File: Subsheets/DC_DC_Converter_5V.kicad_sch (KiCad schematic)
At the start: 30 parts

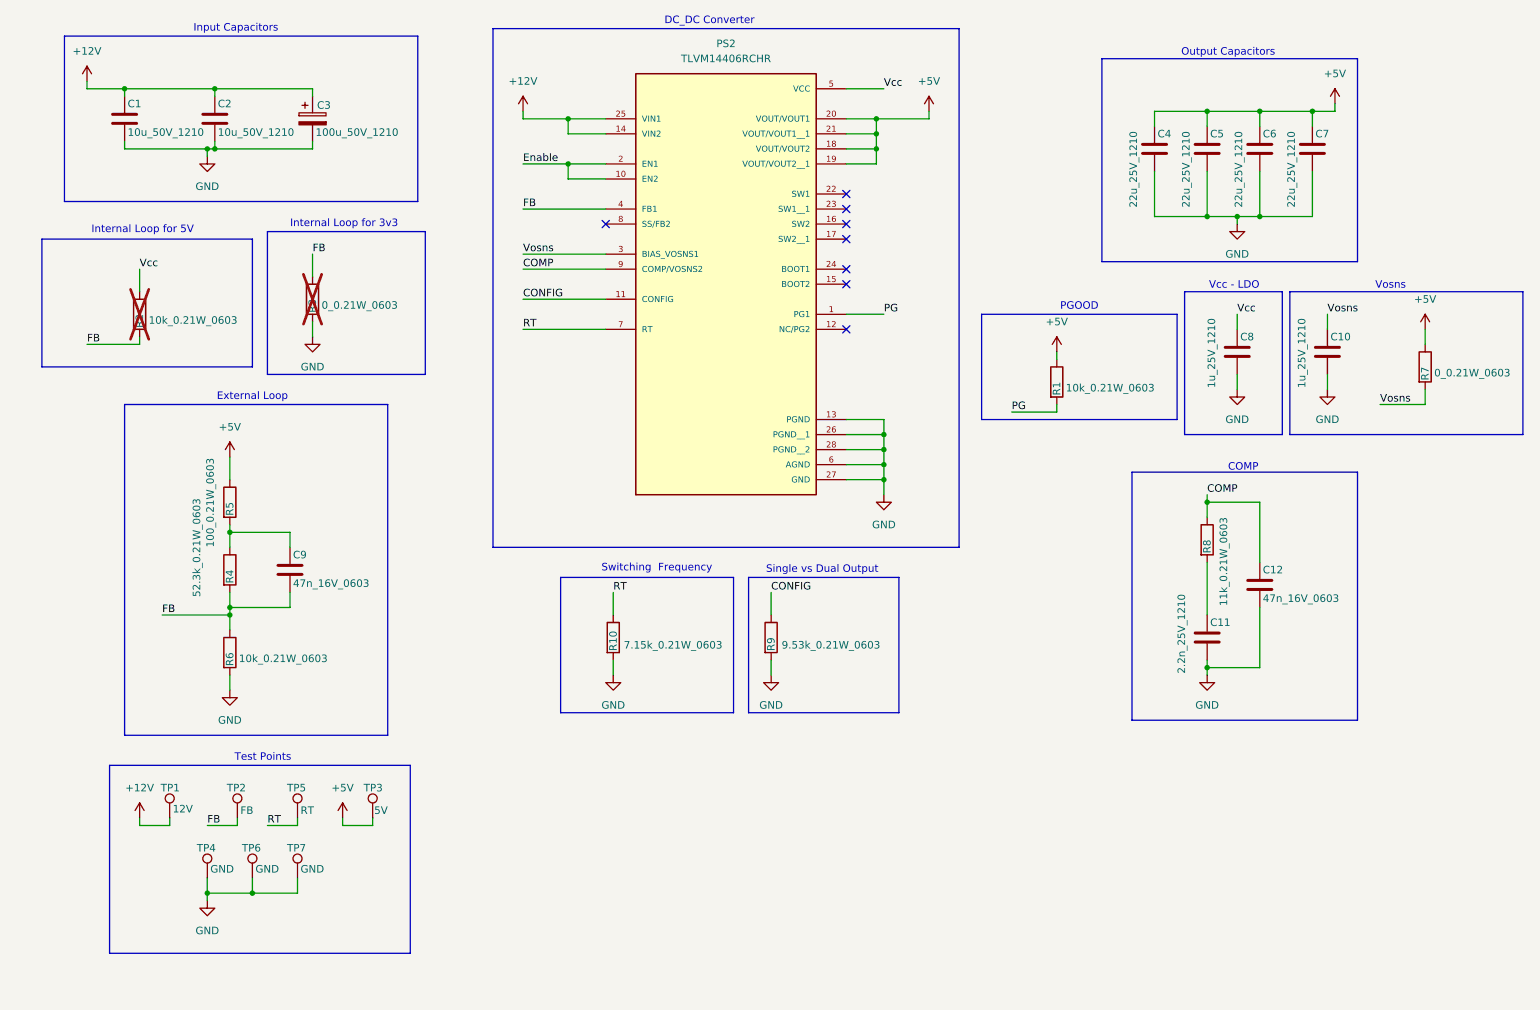
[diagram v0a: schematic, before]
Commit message: Layout import and schema fixes.
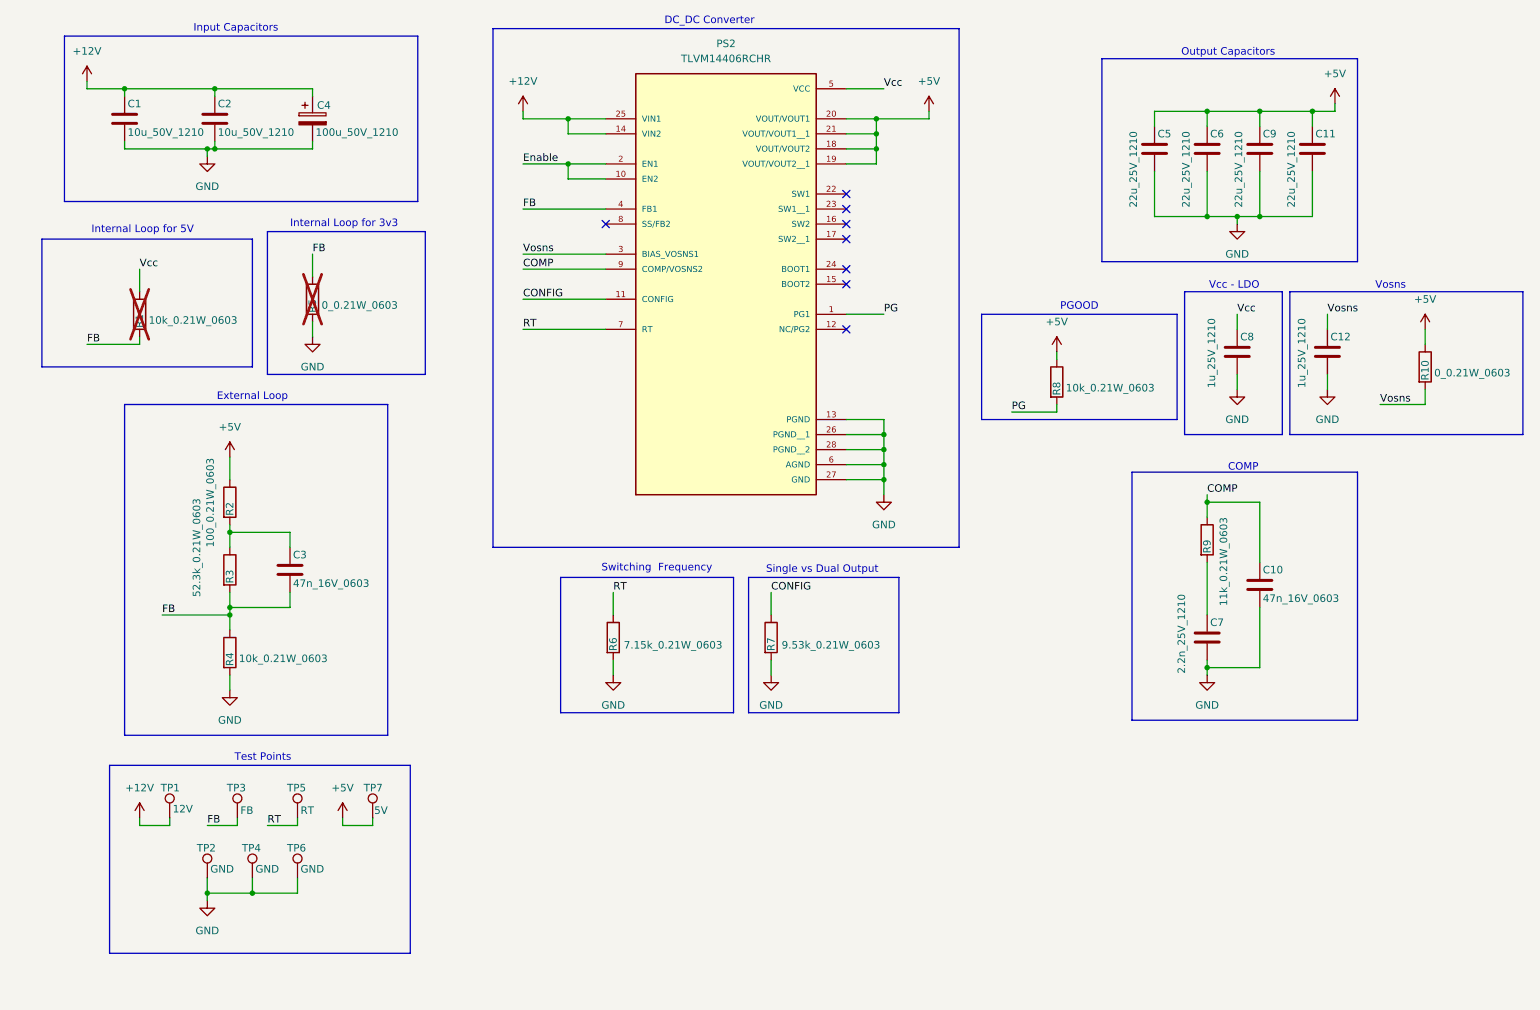
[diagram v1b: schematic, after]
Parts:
- C7: renamed from C11; footprint (none) -> Capacitor_SMD:C_1210_3225Metric
- PS2: footprint TLVM14406RCHR:CONV_TLVM14406RCHR -> footprints:CONV_TLVM14406RCHR; Manufacturer Part Number (none) -> TLVM14406RCHR; Price (none) -> 742; Vendor Link (none) -> https://www.digikey.in/en/products/detail/texas-instruments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; Vendor Part Number (none) -> 296-TLVM14406RCHRCT-ND
- R1: renamed from R2; footprint (none) -> Resistor_SMD:R_0603_1608Metric_Pad0.98x0.95mm_HandSolder; MANUFACTURER (none) -> Vishay Dale; Manufacturer Part Number (none) -> CRCW060310K0FKEAHP; Price (none) -> 6.01; Vendor Link (none) -> https://www.digikey.in/en/products/detail/vishay-dale/CRCW0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; Vendor Part Number (none) -> 541-10.0KSCT-ND
- R10: renamed from R7; footprint (none) -> Resistor_SMD:R_0603_1608Metric_Pad0.98x0.95mm_HandSolder; MANUFACTURER (none) -> Vishay Dale; Manufacturer Part Number (none) -> CRCW06030000Z0EAHP; Price (none) -> 4.86; Vendor Link (none) -> https://www.digikey.in/en/products/detail/vishay-dale/CRCW0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; Vendor Part Number (none) -> 541-0.0SBCT-ND
- R2: renamed from R5; footprint (none) -> Resistor_SMD:R_0603_1608Metric_Pad0.98x0.95mm_HandSolder; MANUFACTURER (none) -> Vishay Dale; Manufacturer Part Number (none) -> CRCW0603100RFKEAHP; Price (none) -> 6.01; Vendor Link (none) -> https://www.digikey.in/en/products/detail/vishay-dale/CRCW0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; Vendor Part Number (none) -> 541-100SCT-ND
- R3: renamed from R4; footprint (none) -> Resistor_SMD:R_0603_1608Metric_Pad0.98x0.95mm_HandSolder; MANUFACTURER (none) -> Vishay Dale; Manufacturer Part Number (none) -> CRCW060352K3FKEAC; Price (none) -> 2.56; Vendor Link (none) -> https://www.digikey.in/en/products/detail/vishay-dale/CRCW0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; Vendor Part Number (none) -> 541-5470-1-ND
- R4: renamed from R6; footprint (none) -> Resistor_SMD:R_0603_1608Metric_Pad0.98x0.95mm_HandSolder; MANUFACTURER (none) -> Vishay Dale; Manufacturer Part Number (none) -> CRCW060310K0FKEAHP; Price (none) -> 6.01; Vendor Link (none) -> https://www.digikey.in/en/products/detail/vishay-dale/CRCW0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; Vendor Part Number (none) -> 541-10.0KSCT-ND
- R5: renamed from R3; footprint (none) -> Resistor_SMD:R_0603_1608Metric_Pad0.98x0.95mm_HandSolder; MANUFACTURER (none) -> Vishay Dale; Manufacturer Part Number (none) -> CRCW06030000Z0EAHP; Price (none) -> 4.86; Vendor Link (none) -> https://www.digikey.in/en/products/detail/vishay-dale/CRCW0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; Vendor Part Number (none) -> 541-0.0SBCT-ND
- R6: renamed from R10; footprint (none) -> Resistor_SMD:R_0603_1608Metric_Pad0.98x0.95mm_HandSolder; MANUFACTURER (none) -> Vishay Dale; Manufacturer Part Number (none) -> CRCW06037K15FKEAHP; Price (none) -> 6.9; Vendor Link (none) -> https://www.digikey.in/en/products/detail/vishay-dale/CRCW0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; Vendor Part Number (none) -> 541-CRCW06037K15FKEAHPCT-ND
- R7: renamed from R9; footprint (none) -> Resistor_SMD:R_0603_1608Metric_Pad0.98x0.95mm_HandSolder; MANUFACTURER (none) -> Vishay Dale; Manufacturer Part Number (none) -> CRCW06039K53FKEAC; Price (none) -> 2.56; Vendor Link (none) -> https://www.digikey.in/en/products/detail/vishay-dale/CRCW0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; Vendor Part Number (none) -> 541-5606-1-ND
- R8: renamed from R1; footprint (none) -> Resistor_SMD:R_0603_1608Metric_Pad0.98x0.95mm_HandSolder; MANUFACTURER (none) -> Vishay Dale; Manufacturer Part Number (none) -> CRCW060310K0FKEAHP; Price (none) -> 6.01; Vendor Link (none) -> https://www.digikey.in/en/products/detail/vishay-dale/CRCW0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; Vendor Part Number (none) -> 541-10.0KSCT-ND
- R9: renamed from R8; footprint (none) -> Resistor_SMD:R_0603_1608Metric_Pad0.98x0.95mm_HandSolder; MANUFACTURER (none) -> Vishay Dale; Manufacturer Part Number (none) -> CRCW060311K0FKEAC; Price (none) -> 2.56; Vendor Link (none) -> https://www.digikey.in/en/products/detail/vishay-dale/CRCW0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; Vendor Part Number (none) -> 541-5146-1-ND
- TP1, TP5: footprint (none) -> TestPoint:TestPoint_Pad_2.0x2.0mm
- TP2: renamed from TP4; footprint (none) -> TestPoint:TestPoint_Pad_2.0x2.0mm
- TP3: renamed from TP2; footprint (none) -> TestPoint:TestPoint_Pad_2.0x2.0mm
- TP4: renamed from TP6; footprint (none) -> TestPoint:TestPoint_Pad_2.0x2.0mm
- TP6: renamed from TP7; footprint (none) -> TestPoint:TestPoint_Pad_2.0x2.0mm
- TP7: renamed from TP3; footprint (none) -> TestPoint:TestPoint_Pad_2.0x2.0mm
- renumbered C12 to C10, C7 to C11, C10 to C12, C9 to C3, C3 to C4, C4 to C5, C5 to C6, C6 to C9

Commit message: layout changes
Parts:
- renumbered TP1 to 12V, TP7 to 5V, TP3 to 5V_FB, TP5 to 5V_RT, TP6 to GND, TP4 to GND, TP2 to GND
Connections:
- net +5V: no longer R8.1
- new net +3V3: R8.1
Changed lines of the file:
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@@
 		(on_board yes)
 		(dnp no)
-		(property "Reference" "TP6"
+		(property "Reference" "GND"
 			(at 69.342 158.75 0)
 			(show_name no)
@@
 			(project "universal-psu"
 				(path "/08cd4a39-b122-4f15-a276-9889e34f331e/c9134cf9-961a-49e2-b7fe-4b733c12d67f"
-					(reference "TP6")
+					(reference "GND")
 					(unit 1)
 				)
@@
 		(on_board yes)
 		(dnp no)
-		(property "Reference" "TP4"
+		(property "Reference" "GND"
 			(at 61.722 158.75 0)
 			(show_name no)
@@
 			(project "universal-psu"
 				(path "/08cd4a39-b122-4f15-a276-9889e34f331e/c9134cf9-961a-49e2-b7fe-4b733c12d67f"
-					(reference "TP4")
+					(reference "GND")
 					(unit 1)
 				)
@@
 		(on_board yes)
 		(dnp no)
-		(property "Reference" "TP2"
+		(property "Reference" "GND"
 			(at 54.102 158.75 0)
 			(show_name no)
@@
 			(project "universal-psu"
 				(path "/08cd4a39-b122-4f15-a276-9889e34f331e/c9134cf9-961a-49e2-b7fe-4b733c12d67f"
-					(reference "TP2")
+					(reference "GND")
 					(unit 1)
 				)
@@
 		(on_board yes)
 		(dnp no)
-		(property "Reference" "TP5"
+		(property "Reference" "5V_RT"
 			(at 69.342 148.59 0)
 			(show_name no)
@@
 			(project "universal-psu"
 				(path "/08cd4a39-b122-4f15-a276-9889e34f331e/c9134cf9-961a-49e2-b7fe-4b733c12d67f"
-					(reference "TP5")
+					(reference "5V_RT")
 					(unit 1)
 				)
@@
 		(on_board yes)
 		(dnp no)
-		(property "Reference" "TP7"
+		(property "Reference" "5V"
 			(at 82.296 148.59 0)
 			(show_name no)
@@
 			(project "universal-psu"
 				(path "/08cd4a39-b122-4f15-a276-9889e34f331e/c9134cf9-961a-49e2-b7fe-4b733c12d67f"
-					(reference "TP7")
+					(reference "5V")
 					(unit 1)
 				)
@@
 		(on_board yes)
 		(dnp no)
-		(property "Reference" "TP1"
+		(property "Reference" "12V"
 			(at 48.006 148.59 0)
 			(show_name no)
@@
 			(project "universal-psu"
 				(path "/08cd4a39-b122-4f15-a276-9889e34f331e/c9134cf9-961a-49e2-b7fe-4b733c12d67f"
-					(reference "TP1")
+					(reference "12V")
+					(unit 1)
+				)
+			)
+		)
+	)
+	(symbol
+		(lib_id "power:+3V3")
+		(at 199.39 74.93 0)
+		(unit 1)
+		(body_style 1)
+		(exclude_from_sim no)
+		(in_bom yes)
+		(on_board yes)
+		(dnp no)
+		(fields_autoplaced yes)
+		(property "Reference" "#PWR047"
+			(at 199.39 78.74 0)
+			(hide yes)
+			(show_name no)
+			(do_not_autoplace no)
+			(effects
+				(font
+					(size 1.27 1.27)
+				)
+			)
+		)
+		(property "Value" "+3V3"
+			(at 199.39 69.85 0)
+			(show_name no)
+			(do_not_autoplace no)
+			(effects
+				(font
+					(size 1.27 1.27)
+				)
+			)
+		)
+		(property "Footprint" ""
+			(at 199.39 74.93 0)
+			(hide yes)
+			(show_name no)
+			(do_not_autoplace no)
+			(effects
+				(font
+					(size 1.27 1.27)
+				)
+			)
+		)
+		(property "Datasheet" ""
+			(at 199.39 74.93 0)
+			(hide yes)
+			(show_name no)
+			(do_not_autoplace no)
+			(effects
+				(font
+					(size 1.27 1.27)
+				)
+			)
+		)
+		(property "Description" "Power symbol creates a global label with name \"+3V3\""
+			(at 199.39 74.93 0)
+			(hide yes)
+			(show_name no)
+			(do_not_autoplace no)
+			(effects
+				(font
+					(size 1.27 1.27)
+				)
+			)
+		)
+		(pin "1"
+		)
+		(instances
+			(project "universal-psu"
+				(path "/08cd4a39-b122-4f15-a276-9889e34f331e/c9134cf9-961a-49e2-b7fe-4b733c12d67f"
+					(reference "#PWR047")
 					(unit 1)
 				)
@@
 		(on_board yes)
 		(dnp no)
-		(property "Reference" "TP3"
+		(property "Reference" "5V_FB"
 			(at 59.182 148.59 0)
 			(show_name no)
@@
 			(project "universal-psu"
 				(path "/08cd4a39-b122-4f15-a276-9889e34f331e/c9134cf9-961a-49e2-b7fe-4b733c12d67f"
-					(reference "TP3")
+					(reference "5V_FB")
 					(unit 1)
 				)
@@
 					(unit 1)
 				)
-			)
-		)
-	)
-	(symbol
-		(lib_id "power:+5V")
-		(at 199.39 74.93 0)
-		(unit 1)
-		(body_style 1)
-		(exclude_from_sim no)
-		(in_bom yes)
-		(on_board yes)
-		(dnp no)
-		(fields_autoplaced yes)
-		(property "Reference" "#PWR020"
-			(at 199.39 78.74 0)
-			(hide yes)
-			(show_name no)
-			(do_not_autoplace no)
-			(effects
-				(font
-					(size 1.27 1.27)
-				)
-			)
-		)
-		(property "Value" "+5V"
-			(at 199.39 69.85 0)
-			(show_name no)
-			(do_not_autoplace no)
-			(effects
-				(font
-					(size 1.27 1.27)
-				)
-			)
-		)
-		(property "Footprint" ""
-			(at 199.39 74.93 0)
-			(hide yes)
-			(show_name no)
-			(do_not_autoplace no)
-			(effects
-				(font
-					(size 1.27 1.27)
-				)
-			)
-		)
-		(property "Datasheet" ""
-			(at 199.39 74.93 0)
-			(hide yes)
-			(show_name no)
-			(do_not_autoplace no)
-			(effects
-				(font
-					(size 1.27 1.27)
-				)
-			)
-		)
-		(property "Description" "Power symbol creates a global label with name \"+5V\""
-			(at 199.39 74.93 0)
-			(hide yes)
-			(show_name no)
-			(do_not_autoplace no)
-			(effects
-				(font
-					(size 1.27 1.27)
-				)
-			)
-		)
-		(pin "1"
-		)
-		(instances
-			(project "universal-psu"
-				(path "/08cd4a39-b122-4f15-a276-9889e34f331e/c9134cf9-961a-49e2-b7fe-4b733c12d67f"
-					(reference "#PWR020")
-					(unit 1)
-				)
